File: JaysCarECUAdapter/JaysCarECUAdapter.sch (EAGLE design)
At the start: 2 parts

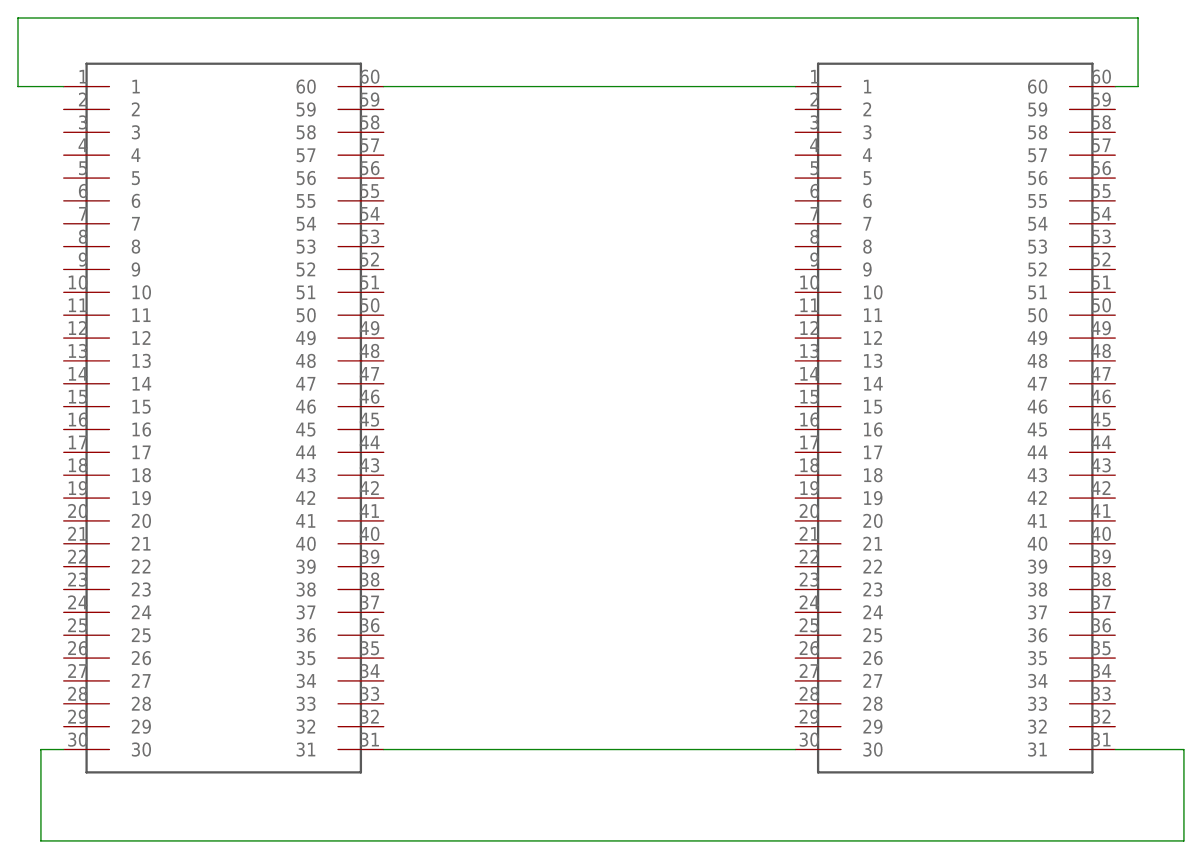
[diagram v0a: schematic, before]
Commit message: Switched to a smaller board, completed the routing.
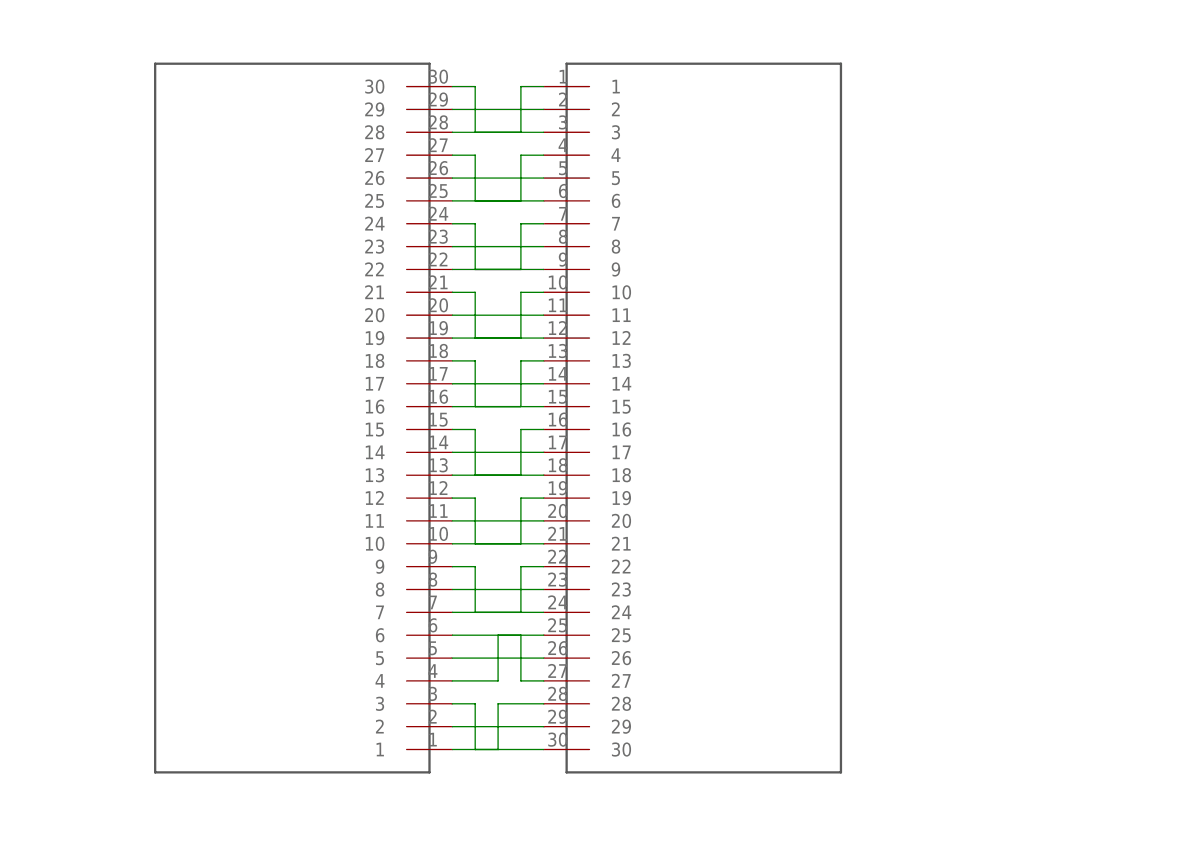
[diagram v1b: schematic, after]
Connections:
- new net N$10: U$1.17, U$2.14
- new net N$11: U$1.16, U$2.13
- new net N$12: U$1.18, U$2.15
- new net N$13: U$1.14, U$2.17
- new net N$14: U$1.13, U$2.16
- new net N$15: U$1.15, U$2.18
- new net N$16: U$1.11, U$2.20
- new net N$17: U$1.10, U$2.19
- new net N$18: U$1.12, U$2.21
- new net N$19: U$1.8, U$2.23
- new net N$20: U$1.9, U$2.24
- new net N$21: U$1.7, U$2.22
- new net N$22: U$1.5, U$2.26
- new net N$23: U$1.4, U$2.25
- new net N$24: U$1.6, U$2.27
- new net N$25: U$1.2, U$2.29
- new net N$26: U$1.3, U$2.30
- new net N$27: U$1.1, U$2.28
- new net N$28: U$1.28, U$2.1
- new net N$29: U$1.29, U$2.2
- new net N$30: U$1.30, U$2.3
- new net N$5: U$1.24, U$2.9
- new net N$6: U$1.22, U$2.7
- new net N$7: U$1.20, U$2.11
- new net N$8: U$1.19, U$2.10
- new net N$9: U$1.21, U$2.12
- net N$1: now also U$1.26, U$2.5; no longer U$1.1, U$2.60
- net N$2: now also U$1.27, U$2.6; no longer U$1.30, U$2.31
- net N$3: now also U$1.25, U$2.4; no longer U$1.31, U$2.30
- net N$4: now also U$1.23, U$2.8; no longer U$1.60, U$2.1
